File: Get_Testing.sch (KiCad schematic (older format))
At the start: 1 part

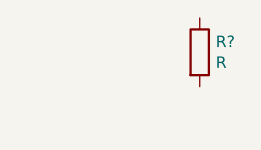
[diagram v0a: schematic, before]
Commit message: Added second resistor
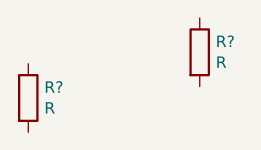
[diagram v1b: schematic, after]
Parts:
- added R?: R, symbol Device:R
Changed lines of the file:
@@
+	1    0    0    -1
+$EndComp
+$Comp
+L Device:R R?
+U 1 1 5F20004D
+P 5500 3300
+F 0 "R?" H 5570 3346 50  0000 L CNN
+F 1 "R" H 5570 3255 50  0000 L CNN
+F 2 "" V 5430 3300 50  0001 C CNN
+F 3 "~" H 5500 3300 50  0001 C CNN
+	1    5500 3300
 	1    0    0    -1
 $EndComp
